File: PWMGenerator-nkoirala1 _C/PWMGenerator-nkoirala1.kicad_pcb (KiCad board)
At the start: 2 copper layers, 30 parts, among them J2 Conn_01x03_Pin, Q2 2N3906, Q4 2N3904, Q5 2N3906, Q6 2N3904, SW1 SW_SPST, U1 LM7805_TO220, U2 LM339

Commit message: commit
fixing some isses
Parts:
- moved D2 102.8 mm to (34.0, 58.0)
- moved D3 102.8 mm to (34.0, 63.0), turned to 180 degrees
- moved D4 94.7 mm to (41.0, 58.0)
- moved D5 94.7 mm to (41.0, 63.0)
- moved F2 0.50 mm to (27.0, 58.0)
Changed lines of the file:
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@@
 	(footprint "Diode_SMD:D_0805_2012Metric_Pad1.15x1.40mm_HandSolder"
 		(layer "F.Cu")
-		(at 135.475 46.5)
+		(at 33.975 63 180)
 		(descr "Diode SMD 0805 (2012 Metric), square (rectangular) end terminal, IPC_7351 nominal, (Body size source: https://docs.google.com/spreadsheets/d/1BsfQQcO9C6DZCsRaXUlFlo91Tg2WpOkGARC1WS5S8t0/edit?usp=sharing), generated with kicad-footprint-generator")
 		(tags "diode handsolder")
 		(property "Reference" "D3"
-			(at 0 -1.65 0)
+			(at 0 -1.65 360)
 			(layer "F.SilkS")
 			(effects
@@
 		)
 		(property "Value" "1N4005G"
-			(at 0 1.65 0)
+			(at 0 1.65 360)
 			(layer "F.Fab")
 			(effects
@@
 		)
 		(property "Footprint" "Diode_SMD:D_0805_2012Metric_Pad1.15x1.40mm_HandSolder"
-			(at 0 0 0)
+			(at 0 0 180)
 			(unlocked yes)
 			(layer "F.Fab")
@@
 		)
 		(property "Datasheet" "http://www.vishay.com/docs/88503/1n4001.pdf"
-			(at 0 0 0)
+			(at 0 0 180)
 			(unlocked yes)
 			(layer "F.Fab")
@@
 		)
 		(property "Description" "600V 1A General Purpose Rectifier Diode, DO-41"
-			(at 0 0 0)
+			(at 0 0 180)
 			(unlocked yes)
 			(layer "F.Fab")
@@
 		)
 		(property "Sim.Device" "D"
-			(at 0 0 0)
+			(at 0 0 180)
 			(unlocked yes)
 			(layer "F.Fab")
@@
 		)
 		(property "Sim.Pins" "1=K 2=A"
-			(at 0 0 0)
+			(at 0 0 180)
 			(unlocked yes)
 			(layer "F.Fab")
@@
 		(attr smd)
 		(fp_line
-			(start -1.86 -0.96)
-			(end -1.86 0.96)
+			(start 1 -0.96)
+			(end -1.86 -0.96)
 			(stroke
 				(width 0.12)
@@
 		)
 		(fp_line
-			(start 1 -0.96)
-			(end -1.86 -0.96)
+			(start -1.86 -0.96)
+			(end -1.86 0.96)
 			(stroke
 				(width 0.12)
@@
 		)
 		(fp_line
-			(start -1.85 -0.95)
-			(end 1.85 -0.95)
+			(start 1.85 0.95)
+			(end -1.85 0.95)
 			(stroke
 				(width 0.05)
@@
 		)
 		(fp_line
-			(start -1.85 0.95)
-			(end -1.85 -0.95)
+			(start 1.85 -0.95)
+			(end 1.85 0.95)
 			(stroke
 				(width 0.05)
@@
 		)
 		(fp_line
-			(start 1.85 -0.95)
-			(end 1.85 0.95)
+			(start -1.85 0.95)
+			(end -1.85 -0.95)
 			(stroke
 				(width 0.05)
@@
 		)
 		(fp_line
-			(start 1.85 0.95)
-			(end -1.85 0.95)
+			(start -1.85 -0.95)
+			(end 1.85 -0.95)
 			(stroke
 				(width 0.05)
@@
 		)
 		(fp_line
-			(start -1 -0.3)
-			(end -1 0.6)
+			(start 1 0.6)
+			(end 1 -0.6)
 			(stroke
 				(width 0.1)
@@
 		)
 		(fp_line
-			(start -1 0.6)
-			(end 1 0.6)
+			(start 1 -0.6)
+			(end -0.7 -0.6)
 			(stroke
 				(width 0.1)
@@
 		)
 		(fp_line
-			(start 1 -0.6)
-			(end -0.7 -0.6)
+			(start -1 0.6)
+			(end 1 0.6)
 			(stroke
 				(width 0.1)
@@
 		)
 		(fp_line
-			(start 1 0.6)
-			(end 1 -0.6)
+			(start -1 -0.3)
+			(end -1 0.6)
 			(stroke
 				(width 0.1)
@@
 		)
 		(fp_text user "${REFERENCE}"
-			(at 0 0 0)
+			(at 0 0 360)
 			(layer "F.Fab")
 			(effects
@@
 		)
 		(pad "1" smd roundrect
-			(at -1.025 0)
+			(at -1.025 0 180)
 			(size 1.15 1.4)
 			(layers "F.Cu" "F.Paste" "F.Mask")
@@
 		)
 		(pad "2" smd roundrect
-			(at 1.025 0)
+			(at 1.025 0 180)
 			(size 1.15 1.4)
 			(layers "F.Cu" "F.Paste" "F.Mask")
@@
 		(tags "Potentiometer vertical Bourns 3296W")
 		(property "Reference" "RV1"
-			(at -2.54 -3.66 360)
+			(at -2.54 -3.66 0)
 			(layer "F.SilkS")
 			(effects
@@
 		)
 		(property "Value" "5kΩ"
-			(at -2.54 3.67 360)
+			(at -2.54 3.67 0)
 			(layer "F.Fab")
 			(effects
@@
 		)
 		(fp_text user "${REFERENCE}"
-			(at -3.175 0.005 360)
+			(at -3.175 0.005 0)
 			(layer "F.Fab")
 			(effects
@@
 		)
 		(fp_text user "${REFERENCE}"
-			(at 2.58 0 360)
+			(at 2.58 0 0)
 			(layer "F.Fab")
 			(effects
@@
 	(footprint "Diode_SMD:D_0805_2012Metric_Pad1.15x1.40mm_HandSolder"
 		(layer "F.Cu")
-		(at 135.475 41.5)
+		(at 33.975 58)
 		(descr "Diode SMD 0805 (2012 Metric), square (rectangular) end terminal, IPC_7351 nominal, (Body size source: https://docs.google.com/spreadsheets/d/1BsfQQcO9C6DZCsRaXUlFlo91Tg2WpOkGARC1WS5S8t0/edit?usp=sharing), generated with kicad-footprint-generator")
 		(tags "diode handsolder")
@@
 	(footprint "NANOSMDC016F-2:RESC3115X65N"
 		(layer "F.Cu")
-		(at 27 58.5)
+		(at 27 58)
 		(descr "<b>RESISTOR</b>")
 		(property "Reference" "F2"
@@
 		)
 		(property "Value" "0.5_AMP"
-			(at 1.223668 1.929681 0)
+			(at 0 1.929681 0)
 			(layer "F.Fab")
 			(effects
@@
 	(footprint "Diode_SMD:D_0805_2012Metric_Pad1.15x1.40mm_HandSolder"
 		(layer "F.Cu")
-		(at 135.475 56.5)
+		(at 40.975 63)
 		(descr "Diode SMD 0805 (2012 Metric), square (rectangular) end terminal, IPC_7351 nominal, (Body size source: https://docs.google.com/spreadsheets/d/1BsfQQcO9C6DZCsRaXUlFlo91Tg2WpOkGARC1WS5S8t0/edit?usp=sharing), generated with kicad-footprint-generator")
 		(tags "diode handsolder")
@@
 		)
 		(property "Value" "1N4005G"
-			(at 0 1.65 0)
+			(at -0.025 2 0)
 			(layer "F.Fab")
 			(effects
@@
 	(footprint "Diode_SMD:D_0805_2012Metric_Pad1.15x1.40mm_HandSolder"
 		(layer "F.Cu")
-		(at 135.475 51.5)
+		(at 40.975 58)
 		(descr "Diode SMD 0805 (2012 Metric), square (rectangular) end terminal, IPC_7351 nominal, (Body size source: https://docs.google.com/spreadsheets/d/1BsfQQcO9C6DZCsRaXUlFlo91Tg2WpOkGARC1WS5S8t0/edit?usp=sharing), generated with kicad-footprint-generator")
 		(tags "diode handsolder")

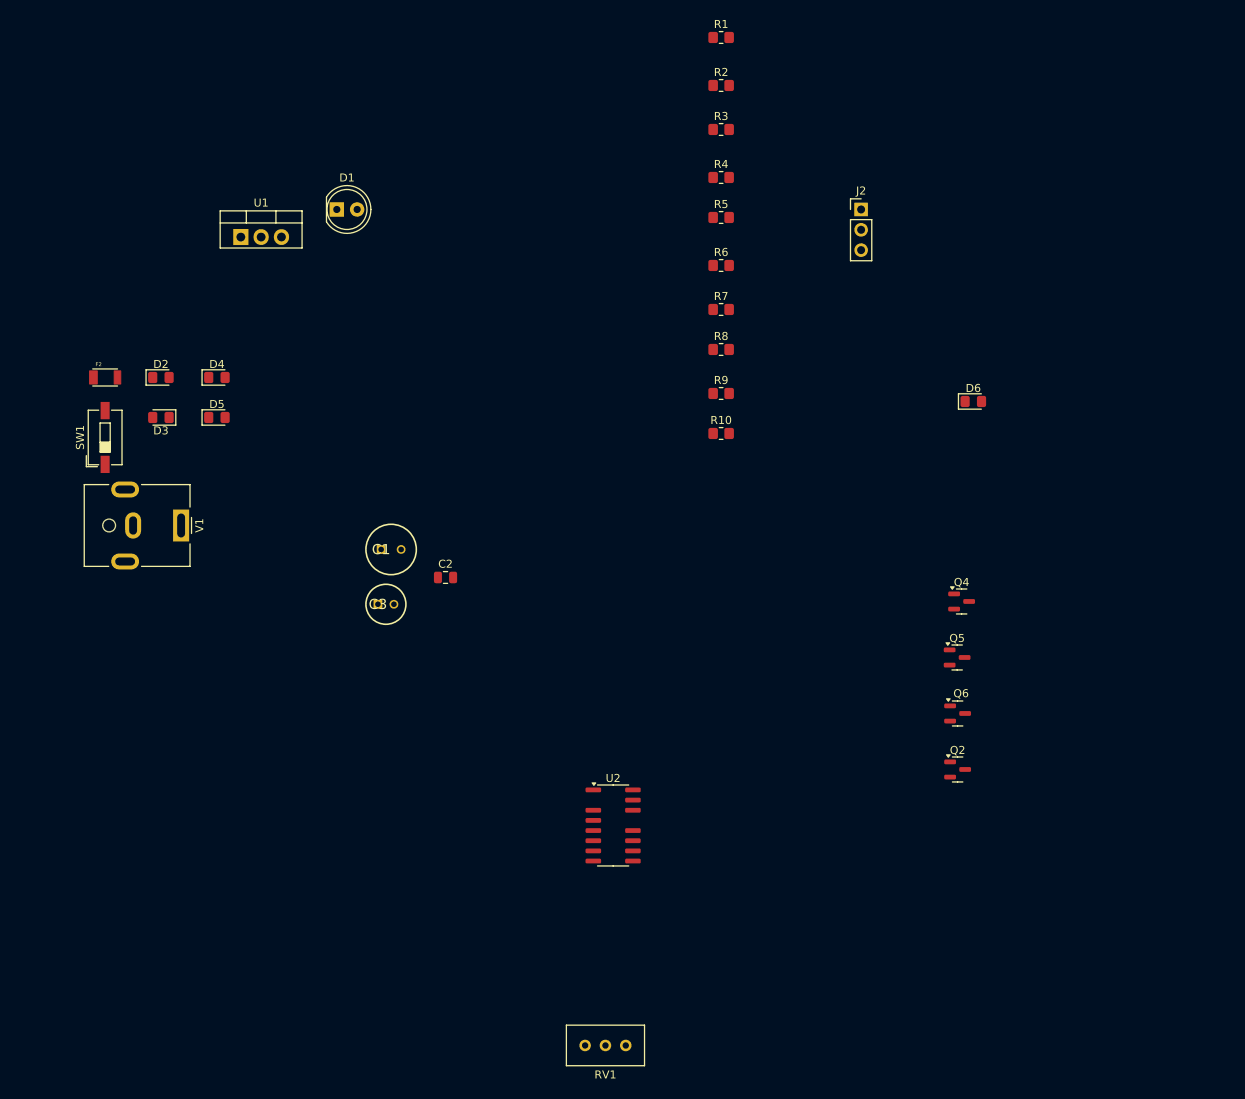
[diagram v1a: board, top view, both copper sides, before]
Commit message: had my footprint wrong fr lm339
Updated
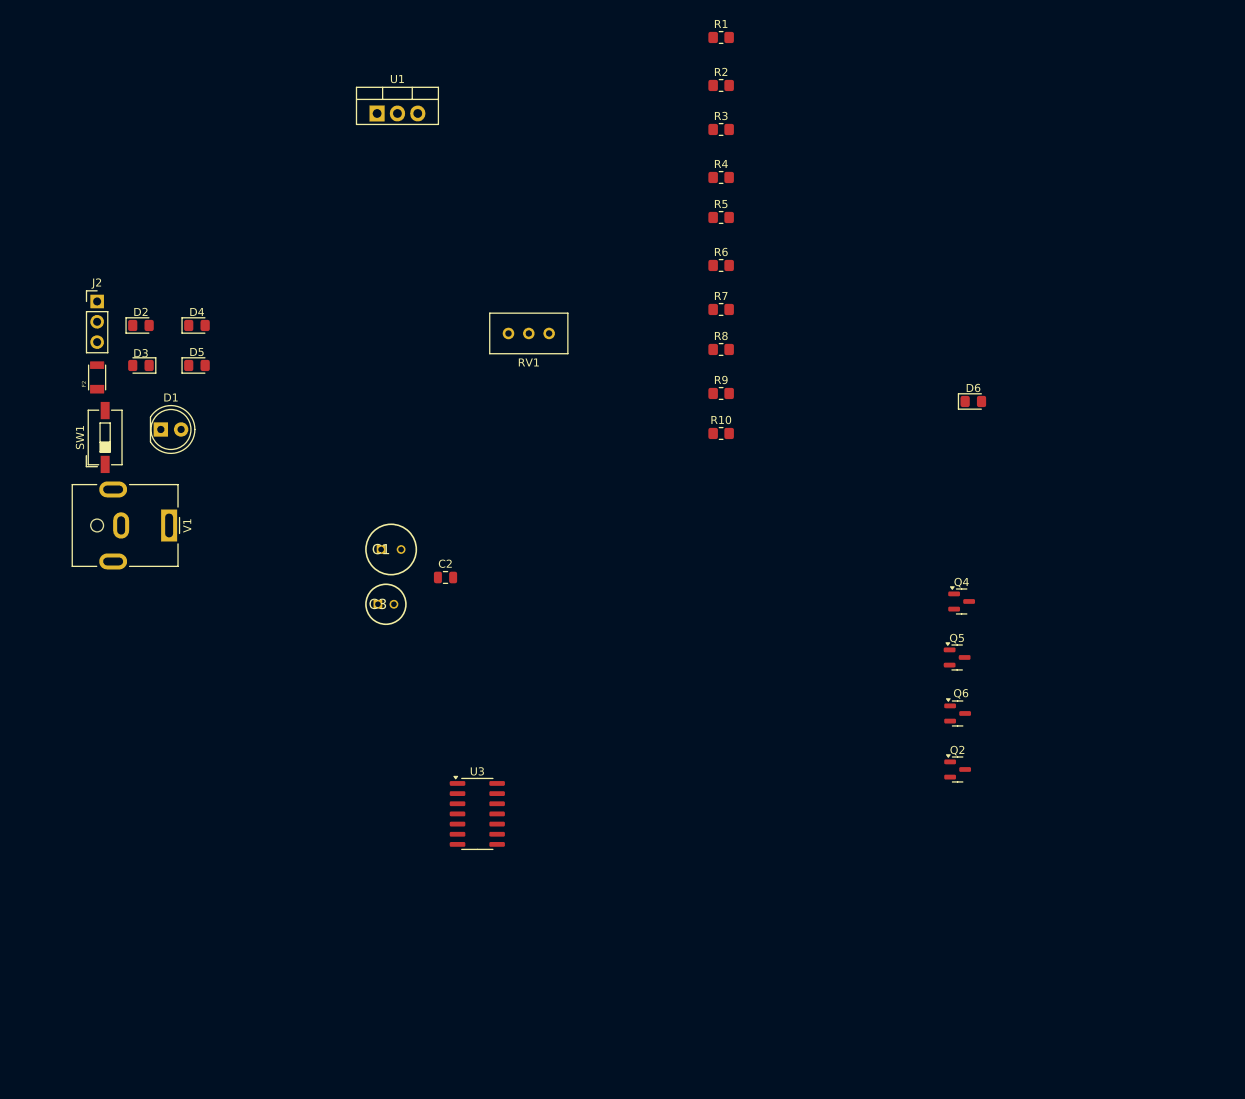
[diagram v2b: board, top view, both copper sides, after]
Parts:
- removed U2: LM339, Package_SO:SOIC-14-16_3.9x9.9mm_P1.27mm
- added U3: LM339, Package_SO:SOIC-14_3.9x8.7mm_P1.27mm, F.Cu at (73.5, 112.6)
- moved J2 96.2 mm to (26.0, 48.5)
- moved RV1 89.5 mm to (77.4, 52.5)
- moved D1 35.2 mm to (34.0, 64.5)
- moved U1 23.0 mm to (61.0, 25.0)
- moved D2 6.96 mm to (31.5, 51.5)
- moved D3 6.96 mm to (31.5, 56.5)
- moved D4 6.96 mm to (38.5, 51.5)
- moved D5 6.96 mm to (38.5, 56.5)
- moved V1 1.50 mm to (35.0, 76.5)
- moved F2 1.00 mm to (26.0, 58.0), turned to 90 degrees

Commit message: commit
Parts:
- moved C1 39.0 mm to (46.5, 43.5)
- moved C2 28.3 mm to (48.5, 64.0)
- moved U1 25.3 mm to (36.5, 31.5), turned to 180 degrees
- moved D3 12.0 mm to (20.0, 53.0)
- moved D5 11.2 mm to (27.5, 54.5), turned to -90 degrees
- moved J2 8.74 mm to (24.0, 40.0), turned to 90 degrees
- moved D2 8.51 mm to (23.5, 48.5), turned to 90 degrees
- moved F2 8.26 mm to (18.0, 60.0)
- moved D4 8.23 mm to (30.5, 49.5), turned to 90 degrees
- moved D1 4.70 mm to (36.5, 60.5), turned to 90 degrees

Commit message: long long drags later
finall one
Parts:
- moved J2 150.0 mm to (161.0, 101.1), turned to 180 degrees
- moved D2 116.7 mm to (122.0, 111.0), turned to -90 degrees
- moved D4 114.7 mm to (126.0, 113.0)
- moved F2 113.5 mm to (122.0, 105.5), turned to -90 degrees
- moved D3 110.8 mm to (117.0, 106.5), turned to 0 degrees
- moved U1 108.7 mm to (125.5, 94.0), turned to 0 degrees
- moved D5 106.1 mm to (116.0, 113.0)
- moved C2 103.8 mm to (140.0, 113.0), turned to -90 degrees
- moved RV1 94.9 mm to (150.9, 112.5)
- moved R1 92.2 mm to (126.0, 105.0), turned to -90 degrees
- moved SW1 88.1 mm to (107.6, 101.0), turned to 0 degrees
- moved C1 87.3 mm to (115.5, 97.0), turned to 90 degrees
- moved R2 82.3 mm to (127.0, 100.5)
- moved U3 80.9 mm to (154.0, 103.8)
- moved R4 79.8 mm to (135.0, 106.5)
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
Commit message: somehow done
thank you
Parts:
- moved R9 12.5 mm to (143.0, 108.5), turned to 90 degrees
- moved C1 12.0 mm to (114.5, 109.0)
- moved C2 12.0 mm to (139.0, 125.0)
- moved C3 12.0 mm to (133.0, 113.5)
- moved D1 12.0 mm to (106.5, 107.0)
- moved D2 12.0 mm to (121.0, 123.0)
- moved D3 12.0 mm to (116.0, 118.5)
- moved D4 12.0 mm to (125.0, 125.0)
- moved D5 12.0 mm to (115.0, 125.0)
- moved D6 12.0 mm to (119.5, 112.5)
- moved F2 12.0 mm to (121.0, 117.5)
- moved J2 12.0 mm to (160.0, 113.1)
- moved Q2 12.0 mm to (140.1, 120.0)
- moved Q4 12.0 mm to (137.1, 108.5)
- moved Q5 12.0 mm to (148.6, 108.4)
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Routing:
- net GND: track 0.00 -> 82.7 mm, vias 0 -> 2
- net VCC: track 0.00 -> 68.6 mm
- net Net-(Q2-C): track 0.00 -> 21.9 mm
- net Net-(D3-K): track 0.00 -> 21.8 mm
- net GNDPWR: track 0.00 -> 20.0 mm
- net Net-(Q4-C): track 0.00 -> 19.3 mm, vias 0 -> 4
- net Net-(U3A-+): track 0.00 -> 17.7 mm, vias 0 -> 2
- net Net-(J2-Pin_2): track 0.00 -> 17.0 mm, vias 0 -> 2
- net Net-(D6-K): track 0.00 -> 16.9 mm, vias 0 -> 1
- net Net-(D1-A): track 0.00 -> 12.4 mm
- net Net-(SW1-B): track 0.00 -> 12.2 mm, vias 0 -> 2
- net Net-(Q2-B): track 0.00 -> 11.3 mm, vias 0 -> 2
- net Net-(Q4-B): track 0.00 -> 10.4 mm, vias 0 -> 2
- net Net-(Q2-E): track 0.00 -> 10.4 mm
- net Net-(R9-Pad1): track 0.00 -> 9.79 mm
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- added copper zone on B.Cu, net GND
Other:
- board outline added: 68 x 33 mm
